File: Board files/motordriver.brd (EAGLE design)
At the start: 30.2 x 44.5 mm, 13 parts, among them Q1 IPB034N03L, U1 VNH5019A

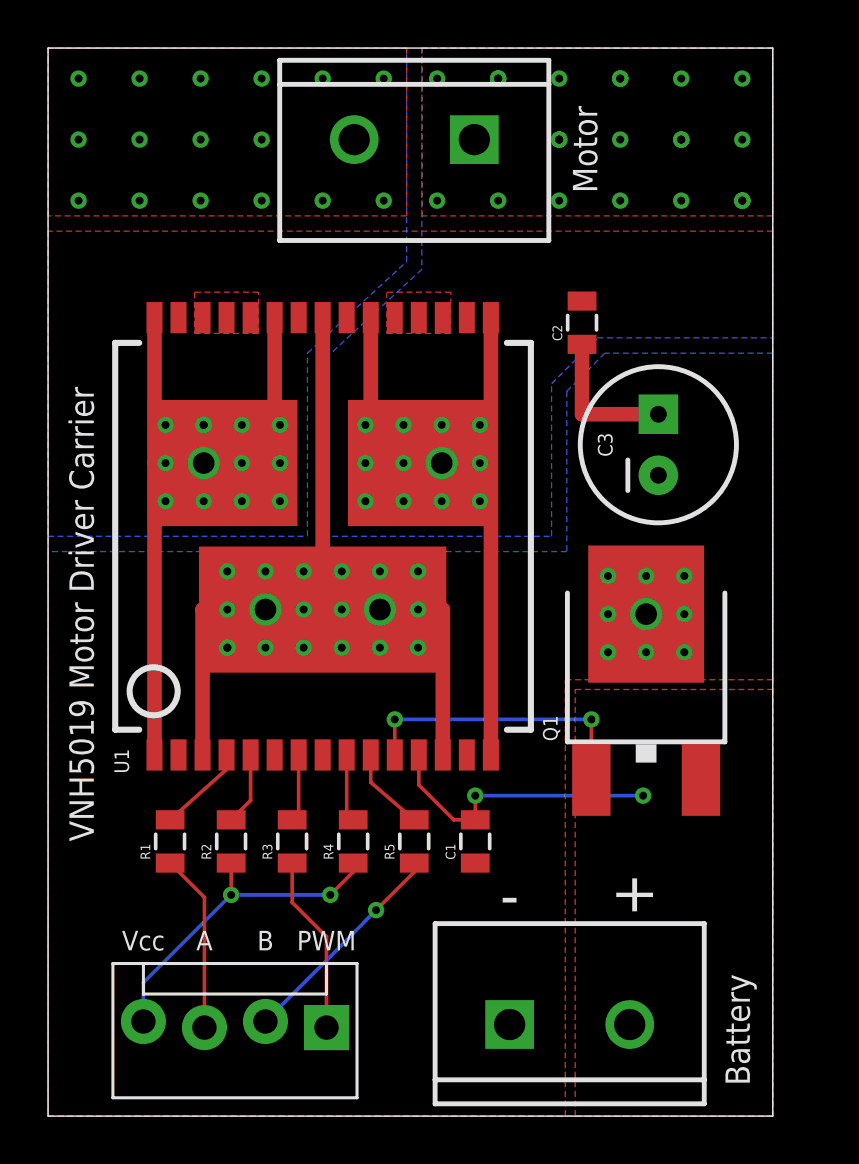
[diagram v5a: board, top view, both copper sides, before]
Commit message: Modified boards to facilitate mounting
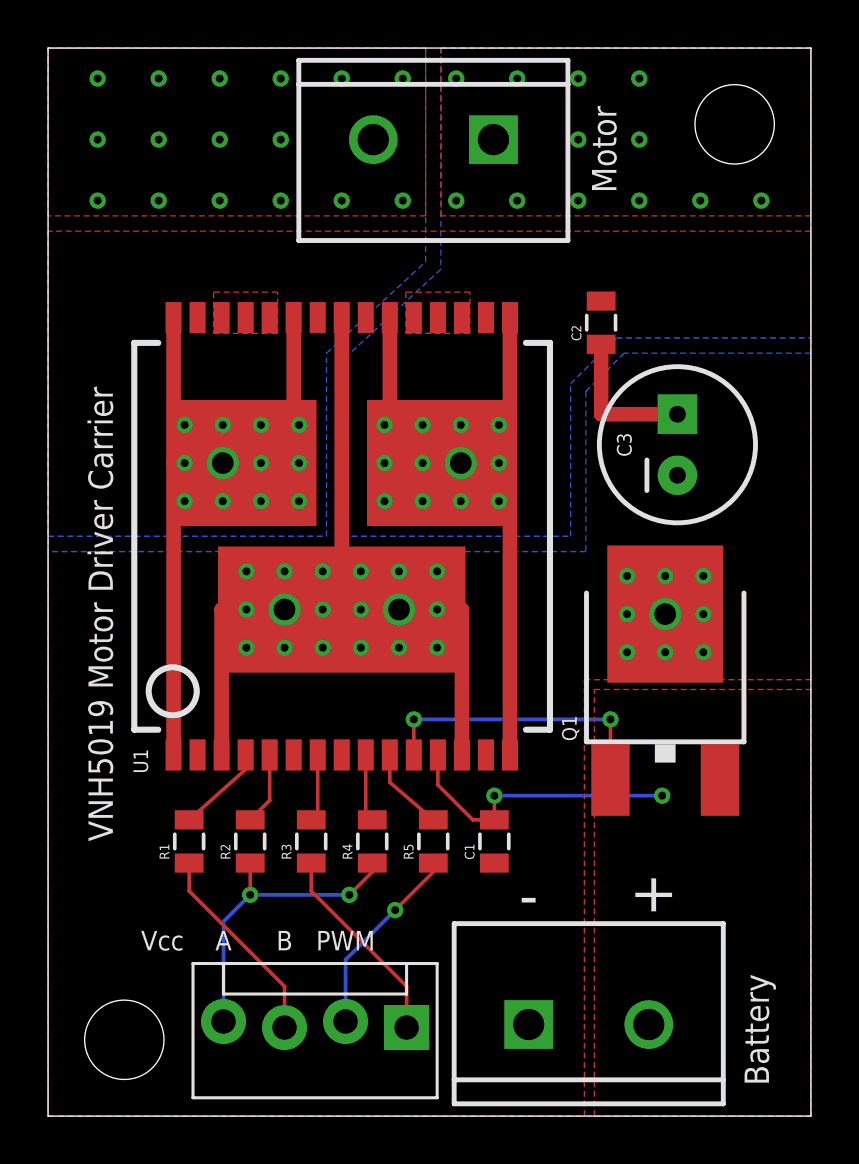
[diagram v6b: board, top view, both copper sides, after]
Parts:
- added STANDOFF1, STANDOFF2: STAND-OFF, SparkFun-Electromechanical:STAND-OFF
- moved JP1 3.33 mm to (14.9, 3.81)
- moved C3 0.79 mm to (26.2, 27.9)
- moved JP2 0.79 mm to (20.0, 3.81)
- moved R4 0.79 mm to (13.5, 11.4)
- moved R5 0.79 mm to (16.0, 11.4)
- moved U1 0.79 mm to (12.2, 24.1)
- moved R1 0.79 mm to (5.87, 11.4)
- moved R2 0.79 mm to (8.41, 11.4)
- moved C1 0.79 mm to (18.6, 11.4)
- moved C2 0.79 mm to (23.0, 33.0)
- moved JP3 0.79 mm to (18.5, 40.6)
- moved Q1 0.79 mm to (25.7, 19.3)
- moved R3 0.79 mm to (11.0, 11.4)
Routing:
- net N$8: track 7.44 -> 8.49 mm
- net N$7: track 7.44 -> 8.49 mm
- net 3.3V: track 13.9 -> 12.9 mm
- net N$5: track 9.15 -> 8.11 mm
- net VCC: vias 28 -> 27
- net OUTB: vias 33 -> 24
- net OUTA: vias 29 -> 28
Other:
- board size 30.2 x 44.5 mm -> 31.8 x 44.5 mm

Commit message: Fixed silkscreen positioning
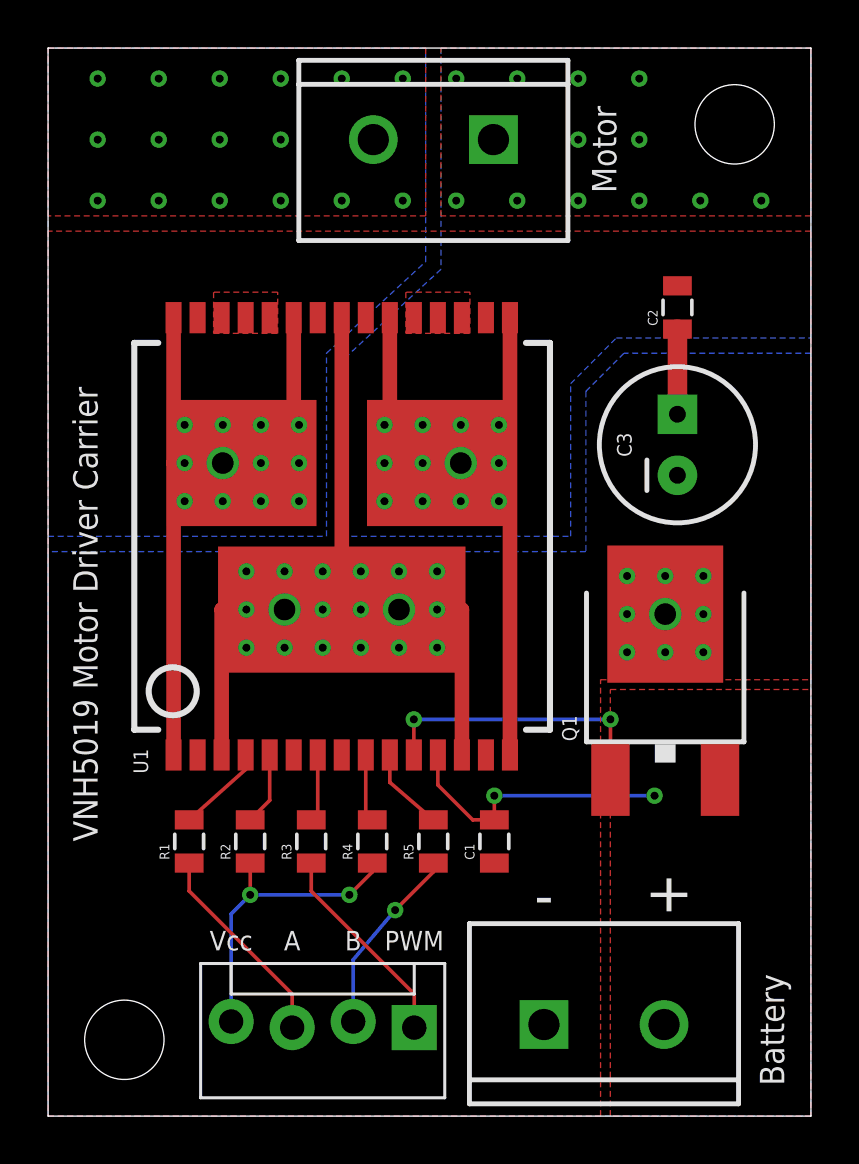
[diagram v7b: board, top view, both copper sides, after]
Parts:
- moved C2 3.24 mm to (26.2, 33.7)
- moved JP2 0.63 mm to (20.6, 3.81)
- moved JP1 0.32 mm to (15.2, 3.81)
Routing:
- net VCC: track 43.8 -> 41.3 mm
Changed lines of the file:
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@@
 <wire x1="31.75" y1="44.45" x2="0" y2="44.45" width="0" layer="20"/>
 <wire x1="0" y1="44.45" x2="0" y2="0" width="0" layer="20"/>
-<text x="2.69875" y="11.43" size="1.016" layer="21" rot="R90">VNH5019 Motor Driver Carrier</text>
-<text x="25.0825" y="9.2075" size="1.778" layer="21" rot="R90" align="center">+</text>
-<text x="20.0025" y="9.2075" size="1.778" layer="21" align="center">-</text>
-<text x="4.7625" y="7.3025" size="0.8128" layer="21" align="center">Vcc</text>
-<text x="7.3025" y="7.3025" size="0.8128" layer="21" align="center">A</text>
-<text x="9.8425" y="7.3025" size="0.8128" layer="21" align="center">B</text>
-<text x="12.3825" y="7.3025" size="0.8128" layer="21" align="center">PWM</text>
-<text x="30.00375" y="1.27" size="1.016" layer="21" rot="R90">Battery</text>
+<text x="2.06375" y="11.43" size="1.016" layer="21" rot="R90">VNH5019 Motor Driver Carrier</text>
+<text x="25.7175" y="9.2075" size="1.778" layer="21" rot="R90" align="center">+</text>
+<text x="20.6375" y="9.2075" size="1.778" layer="21" align="center">-</text>
+<text x="7.62" y="7.3025" size="0.8128" layer="21" align="center">Vcc</text>
+<text x="10.16" y="7.3025" size="0.8128" layer="21" align="center">A</text>
+<text x="12.7" y="7.3025" size="0.8128" layer="21" align="center">B</text>
+<text x="15.24" y="7.3025" size="0.8128" layer="21" align="center">PWM</text>
+<text x="30.63875" y="1.27" size="1.016" layer="21" rot="R90">Battery</text>
 <text x="23.65375" y="38.4175" size="1.016" layer="21" rot="R90">Motor</text>
 </plain>
@@
 <attribute name="NAME" x="4.16375" y="14.255" size="0.6096" layer="25" rot="R90"/>
 </element>
-<element name="JP2" library="SparkFun-Connectors" package="SCREWTERMINAL-5MM-2" value="BATTERY" x="20.0025" y="3.81" smashed="yes"/>
+<element name="JP2" library="SparkFun-Connectors" package="SCREWTERMINAL-5MM-2" value="BATTERY" x="20.6375" y="3.81" smashed="yes"/>
 <element name="JP3" library="SparkFun-Connectors" package="SCREWTERMINAL-5MM-2" value="MOTOR" x="18.53565" y="40.64" smashed="yes" rot="R180"/>
 <element name="Q1" library="SparkFun-DiscreteSemi" package="DPAK" value="IPB034N03L" x="25.68575" y="19.304" smashed="yes">
@@
 </element>
 <element name="C1" library="SparkFun-Capacitors" package="0805" value="0.1uF" x="18.57375" y="11.43" rot="R90"/>
-<element name="C2" library="SparkFun-Capacitors" package="0805" value="0.1uF" x="23.01875" y="33.02" rot="R90"/>
+<element name="C2" library="SparkFun-Capacitors" package="0805" value="0.1uF" x="26.19375" y="33.655" rot="R90"/>
 <element name="C3" library="SparkFun-Capacitors" package="CPOL-RADIAL-100UF-25V" value="47uF" x="26.19375" y="27.94" smashed="yes" rot="R90">
 <attribute name="NAME" x="24.28875" y="27.94" size="0.6096" layer="25" rot="R90" align="bottom-center"/>
@@
 <element name="R2" library="SparkFun-Resistors" package="0805" value="1k" x="8.41375" y="11.43" rot="R90"/>
 <element name="R4" library="SparkFun-Resistors" package="0805" value="1k" x="13.49375" y="11.43" rot="R90"/>
-<element name="JP1" library="SparkFun-Connectors" package="MOLEX-1X4_LOCK" value="" x="14.9225" y="3.81" rot="R180"/>
+<element name="JP1" library="SparkFun-Connectors" package="MOLEX-1X4_LOCK" value="" x="15.24" y="3.81" rot="R180"/>
 <element name="STANDOFF1" library="SparkFun-Electromechanical" package="STAND-OFF" value="STAND-OFF" x="3.175" y="3.175"/>
 <element name="STANDOFF2" library="SparkFun-Electromechanical" package="STAND-OFF" value="STAND-OFF" x="28.575" y="41.275"/>
@@
 <polygon width="0.254" layer="1">
 <vertex x="0" y="0"/>
-<vertex x="22.32025" y="0"/>
-<vertex x="22.32025" y="18.161"/>
+<vertex x="22.99335" y="0"/>
+<vertex x="22.99335" y="18.161"/>
 <vertex x="31.75" y="18.161"/>
 <vertex x="31.75" y="36.83"/>
@@
 <polygon width="0.254" layer="1">
 <vertex x="31.75" y="0"/>
-<vertex x="22.733" y="0"/>
-<vertex x="22.733" y="17.7546"/>
+<vertex x="23.39975" y="0"/>
+<vertex x="23.39975" y="17.7546"/>
 <vertex x="31.75" y="17.7546"/>
 </polygon>
 <wire x1="18.57375" y1="12.33" x2="18.57375" y2="13.335" width="0.1524" layer="1"/>
 <via x="18.57375" y="13.335" extent="1-16" drill="0.3302"/>
-<wire x1="18.57375" y1="13.335" x2="25.55875" y2="13.335" width="0.1524" layer="16"/>
-<via x="25.55875" y="13.335" extent="1-16" drill="0.3302"/>
+<wire x1="18.57375" y1="13.335" x2="25.24125" y2="13.335" width="0.1524" layer="16"/>
+<via x="25.24125" y="13.335" extent="1-16" drill="0.3302"/>
 </signal>
 <signal name="OUTB">
@@
 <wire x1="12.22375" y1="21.08" x2="17.22375" y2="21.08" width="0.6096" layer="1"/>
 <wire x1="17.22375" y1="21.08" x2="17.22375" y2="15.03" width="0.6096" layer="1"/>
-<wire x1="23.01875" y1="32.12" x2="23.01875" y2="29.21" width="0.6096" layer="1"/>
-<wire x1="23.01875" y1="29.21" x2="26.19375" y2="29.21" width="0.6096" layer="1"/>
 <polygon width="0.254" layer="16">
 <vertex x="0" y="0"/>
@@
 <wire x1="26.19375" y1="20.32" x2="26.19375" y2="20.892" width="0.1524" layer="1"/>
 <wire x1="26.19375" y1="20.892" x2="25.68575" y2="20.892" width="0.1524" layer="1"/>
+<wire x1="26.19375" y1="32.755" x2="26.19375" y2="29.21" width="0.8128" layer="1"/>
 </signal>
 <signal name="3.3V">
@@
 <wire x1="12.54125" y1="9.2075" x2="8.41375" y2="9.2075" width="0.1524" layer="16"/>
 <contactref element="JP1" pad="4"/>
-<wire x1="8.41375" y1="9.2075" x2="7.3025" y2="8.09625" width="0.1524" layer="16"/>
-<wire x1="7.3025" y1="8.09625" x2="7.3025" y2="3.937" width="0.1524" layer="16"/>
+<wire x1="8.41375" y1="9.2075" x2="7.62" y2="8.41375" width="0.1524" layer="16"/>
+<wire x1="7.62" y1="8.41375" x2="7.62" y2="3.937" width="0.1524" layer="16"/>
 </signal>
 <signal name="N$1">
@@
 <wire x1="14.44625" y1="8.5725" x2="16.03375" y2="10.16" width="0.1524" layer="1"/>
 <wire x1="16.03375" y1="10.16" x2="16.03375" y2="10.53" width="0.1524" layer="1"/>
-<wire x1="14.44625" y1="8.5725" x2="12.3825" y2="6.50875" width="0.1524" layer="16"/>
-<wire x1="12.3825" y1="6.50875" x2="12.3825" y2="3.937" width="0.1524" layer="16"/>
+<wire x1="14.44625" y1="8.5725" x2="12.7" y2="6.50875" width="0.1524" layer="16"/>
+<wire x1="12.7" y1="6.50875" x2="12.7" y2="3.937" width="0.1524" layer="16"/>
 </signal>
 <signal name="N$7">
@@
 <contactref element="JP1" pad="3"/>
 <wire x1="5.87375" y1="10.53" x2="5.87375" y2="9.36625" width="0.1524" layer="1"/>
-<wire x1="5.87375" y1="9.36625" x2="9.8425" y2="5.3975" width="0.1524" layer="1"/>
-<wire x1="9.8425" y1="5.3975" x2="9.8425" y2="3.683" width="0.1524" layer="1"/>
+<wire x1="5.87375" y1="9.36625" x2="10.16" y2="5.08" width="0.1524" layer="1"/>
+<wire x1="10.16" y1="5.08" x2="10.16" y2="3.683" width="0.1524" layer="1"/>
 </signal>
 <signal name="N$8">
@@
 <contactref element="JP1" pad="1"/>
 <wire x1="10.95375" y1="10.53" x2="10.95375" y2="9.36625" width="0.1524" layer="1"/>
-<wire x1="10.95375" y1="9.36625" x2="14.9225" y2="5.3975" width="0.1524" layer="1"/>
-<wire x1="14.9225" y1="5.3975" x2="14.9225" y2="3.683" width="0.1524" layer="1"/>
+<wire x1="10.95375" y1="9.36625" x2="15.24" y2="5.08" width="0.1524" layer="1"/>
+<wire x1="15.24" y1="5.08" x2="15.24" y2="3.683" width="0.1524" layer="1"/>
 </signal>
 <signal name="N$9">

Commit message: Moved some components
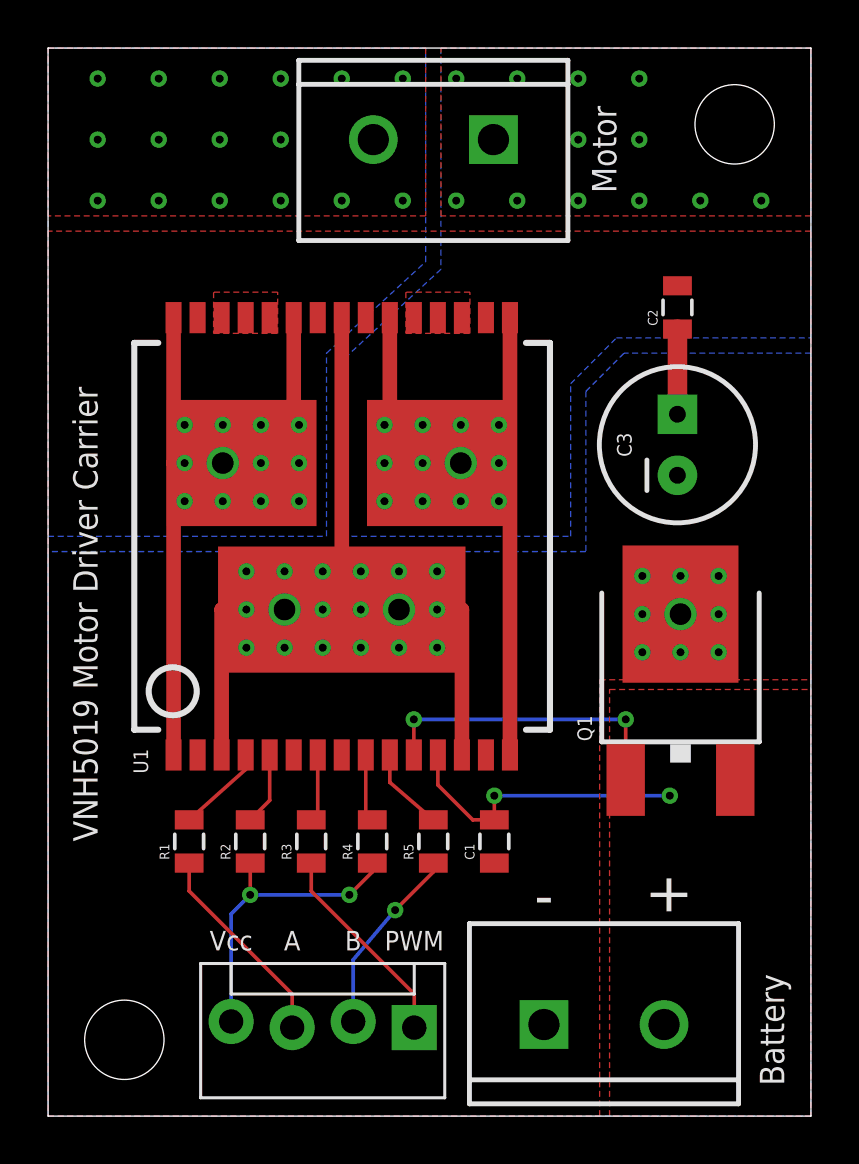
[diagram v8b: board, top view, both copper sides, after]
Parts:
- moved Q1 0.64 mm to (26.3, 19.3)
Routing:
- net VIN: track 12.2 -> 12.8 mm
- net N$4: track 12.2 -> 12.8 mm
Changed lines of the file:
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@@
 <element name="JP2" library="SparkFun-Connectors" package="SCREWTERMINAL-5MM-2" value="BATTERY" x="20.6375" y="3.81" smashed="yes"/>
 <element name="JP3" library="SparkFun-Connectors" package="SCREWTERMINAL-5MM-2" value="MOTOR" x="18.53565" y="40.64" smashed="yes" rot="R180"/>
-<element name="Q1" library="SparkFun-DiscreteSemi" package="DPAK" value="IPB034N03L" x="25.68575" y="19.304" smashed="yes">
-<attribute name="PROD_ID" value="TRANS-09984" x="25.68575" y="19.304" size="1.778" layer="27" display="off"/>
-<attribute name="NAME" x="22.00275" y="15.602" size="0.6096" layer="25" rot="R90"/>
+<element name="Q1" library="SparkFun-DiscreteSemi" package="DPAK" value="IPB034N03L" x="26.32075" y="19.304" smashed="yes">
+<attribute name="PROD_ID" value="TRANS-09984" x="26.32075" y="19.304" size="1.778" layer="27" display="off"/>
+<attribute name="NAME" x="22.63775" y="15.602" size="0.6096" layer="25" rot="R90"/>
 </element>
 <element name="C1" library="SparkFun-Capacitors" package="0805" value="0.1uF" x="18.57375" y="11.43" rot="R90"/>
@@
 <polygon width="0.254" layer="1">
 <vertex x="0" y="0"/>
-<vertex x="22.99335" y="0"/>
-<vertex x="22.99335" y="18.161"/>
+<vertex x="22.95525" y="0"/>
+<vertex x="22.95525" y="18.161"/>
 <vertex x="31.75" y="18.161"/>
 <vertex x="31.75" y="36.83"/>
@@
 <polygon width="0.254" layer="1">
 <vertex x="31.75" y="0"/>
-<vertex x="23.39975" y="0"/>
-<vertex x="23.39975" y="17.7546"/>
+<vertex x="23.368" y="0"/>
+<vertex x="23.368" y="17.7546"/>
 <vertex x="31.75" y="17.7546"/>
 </polygon>
 <wire x1="18.57375" y1="12.33" x2="18.57375" y2="13.335" width="0.1524" layer="1"/>
 <via x="18.57375" y="13.335" extent="1-16" drill="0.3302"/>
-<wire x1="18.57375" y1="13.335" x2="25.24125" y2="13.335" width="0.1524" layer="16"/>
-<via x="25.24125" y="13.335" extent="1-16" drill="0.3302"/>
+<wire x1="18.57375" y1="13.335" x2="25.87625" y2="13.335" width="0.1524" layer="16"/>
+<via x="25.87625" y="13.335" extent="1-16" drill="0.3302"/>
 </signal>
 <signal name="OUTB">
@@
 <wire x1="15.22375" y1="15.03" x2="15.22375" y2="16.51" width="0.1524" layer="1"/>
 <via x="15.22375" y="16.51" extent="1-16" drill="0.3302"/>
-<wire x1="15.22375" y1="16.51" x2="23.40575" y2="16.51" width="0.1524" layer="16"/>
-<via x="23.40575" y="16.51" extent="1-16" drill="0.3302"/>
-<wire x1="23.40575" y1="16.51" x2="23.40575" y2="13.994" width="0.1524" layer="1"/>
+<wire x1="15.22375" y1="16.51" x2="24.04075" y2="16.51" width="0.1524" layer="16"/>
+<via x="24.04075" y="16.51" extent="1-16" drill="0.3302"/>
+<wire x1="24.04075" y1="16.51" x2="24.04075" y2="13.994" width="0.1524" layer="1"/>
 </signal>
 <signal name="VCC">
@@
 <wire x1="13.0175" y1="21.082" x2="13.0175" y2="21.59" width="0.1524" layer="1"/>
 <wire x1="13.0175" y1="21.59" x2="12.22375" y2="21.59" width="0.1524" layer="1"/>
-<via x="25.68575" y="19.304" extent="1-16" drill="0.3302"/>
-<via x="24.09825" y="19.304" extent="1-16" drill="0.3302"/>
-<via x="27.27325" y="19.304" extent="1-16" drill="0.3302"/>
-<via x="27.27325" y="20.8915" extent="1-16" drill="0.3302"/>
-<via x="25.68575" y="20.8915" extent="1-16" drill="0.9"/>
-<via x="24.09825" y="20.8915" extent="1-16" drill="0.3302"/>
-<via x="24.09825" y="22.479" extent="1-16" drill="0.3302"/>
-<via x="25.68575" y="22.479" extent="1-16" drill="0.3302"/>
-<via x="27.27325" y="22.479" extent="1-16" drill="0.3302"/>
-<wire x1="25.68575" y1="20.8915" x2="25.68575" y2="20.32" width="0.1524" layer="1"/>
-<wire x1="25.68575" y1="20.32" x2="26.19375" y2="20.32" width="0.1524" layer="1"/>
-<wire x1="26.19375" y1="20.32" x2="26.19375" y2="20.892" width="0.1524" layer="1"/>
-<wire x1="26.19375" y1="20.892" x2="25.68575" y2="20.892" width="0.1524" layer="1"/>
+<via x="26.32075" y="19.304" extent="1-16" drill="0.3302"/>
+<via x="24.73325" y="19.304" extent="1-16" drill="0.3302"/>
+<via x="27.90825" y="19.304" extent="1-16" drill="0.3302"/>
+<via x="27.90825" y="20.8915" extent="1-16" drill="0.3302"/>
+<via x="26.32075" y="20.8915" extent="1-16" drill="0.9"/>
+<via x="24.73325" y="20.8915" extent="1-16" drill="0.3302"/>
+<via x="24.73325" y="22.479" extent="1-16" drill="0.3302"/>
+<via x="26.32075" y="22.479" extent="1-16" drill="0.3302"/>
+<via x="27.90825" y="22.479" extent="1-16" drill="0.3302"/>
+<wire x1="26.32075" y1="20.8915" x2="26.32075" y2="20.32" width="0.1524" layer="1"/>
+<wire x1="26.32075" y1="20.32" x2="26.82875" y2="20.32" width="0.1524" layer="1"/>
+<wire x1="26.82875" y1="20.32" x2="26.82875" y2="20.892" width="0.1524" layer="1"/>
+<wire x1="26.82875" y1="20.892" x2="26.32075" y2="20.892" width="0.1524" layer="1"/>
 <wire x1="26.19375" y1="32.755" x2="26.19375" y2="29.21" width="0.8128" layer="1"/>
 </signal>
